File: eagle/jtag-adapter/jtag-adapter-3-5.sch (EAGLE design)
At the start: 40 parts, among them IC1 REG1117, Q1 BSS84, Q2 BSS123, X1 TAGCONNECT, X3 CC3220SF-JTAG-HAT, X5 JTAG-IN, X7 MICRO-USB-B

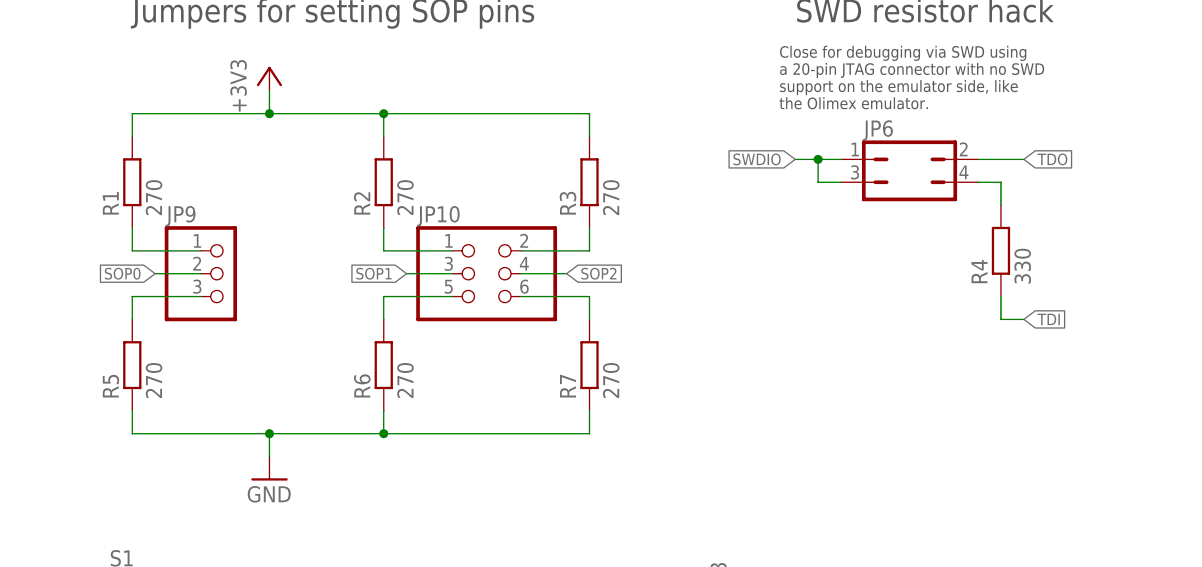
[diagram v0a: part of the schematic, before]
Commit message: Updates resistor values.
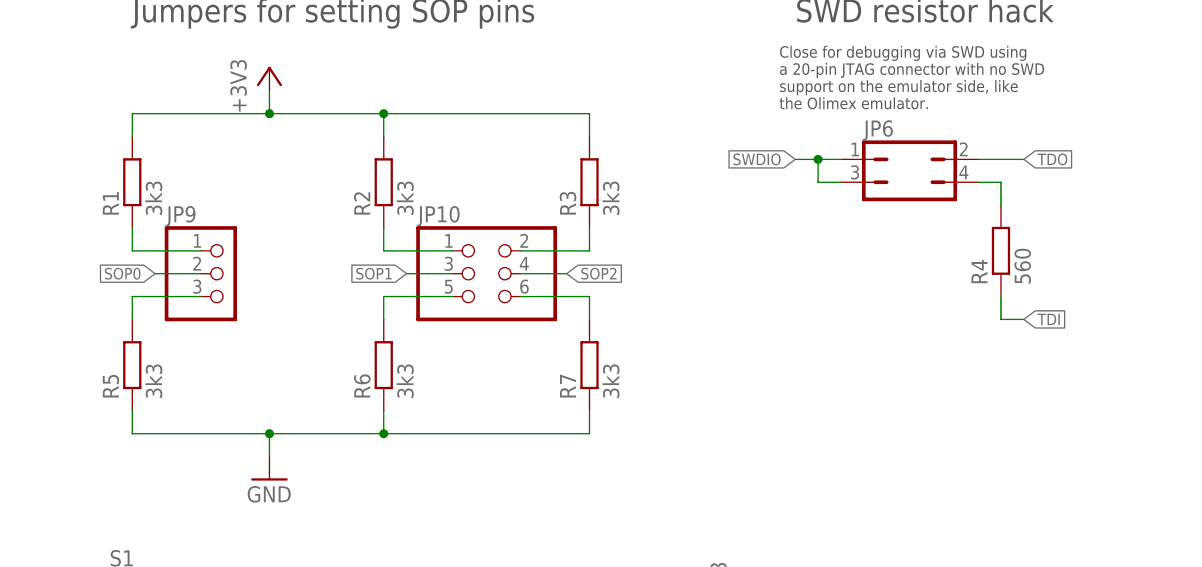
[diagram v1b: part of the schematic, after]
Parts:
- R1, R2, R3, R5, R6, R7: value 270 -> 3k3
- R4: value 330 -> 560
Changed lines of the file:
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@@
 <part name="FRAME1" library="tcs" deviceset="FRAME_A_L" device=""/>
 <part name="JP9" library="adafruit" deviceset="PINHD-1X3" device=""/>
-<part name="R1" library="rcl" library_urn="urn:adsk.eagle:library:334" deviceset="R-EU_" device="R0805" package3d_urn="urn:adsk.eagle:package:23553/2" value="270"/>
-<part name="R2" library="rcl" library_urn="urn:adsk.eagle:library:334" deviceset="R-EU_" device="R0805" package3d_urn="urn:adsk.eagle:package:23553/2" value="270"/>
-<part name="R3" library="rcl" library_urn="urn:adsk.eagle:library:334" deviceset="R-EU_" device="R0805" package3d_urn="urn:adsk.eagle:package:23553/2" value="270"/>
-<part name="R5" library="rcl" library_urn="urn:adsk.eagle:library:334" deviceset="R-EU_" device="R0805" package3d_urn="urn:adsk.eagle:package:23553/2" value="270"/>
-<part name="R6" library="rcl" library_urn="urn:adsk.eagle:library:334" deviceset="R-EU_" device="R0805" package3d_urn="urn:adsk.eagle:package:23553/2" value="270"/>
-<part name="R7" library="rcl" library_urn="urn:adsk.eagle:library:334" deviceset="R-EU_" device="R0805" package3d_urn="urn:adsk.eagle:package:23553/2" value="270"/>
+<part name="R1" library="rcl" library_urn="urn:adsk.eagle:library:334" deviceset="R-EU_" device="R0805" package3d_urn="urn:adsk.eagle:package:23553/2" value="3k3"/>
+<part name="R2" library="rcl" library_urn="urn:adsk.eagle:library:334" deviceset="R-EU_" device="R0805" package3d_urn="urn:adsk.eagle:package:23553/2" value="3k3"/>
+<part name="R3" library="rcl" library_urn="urn:adsk.eagle:library:334" deviceset="R-EU_" device="R0805" package3d_urn="urn:adsk.eagle:package:23553/2" value="3k3"/>
+<part name="R5" library="rcl" library_urn="urn:adsk.eagle:library:334" deviceset="R-EU_" device="R0805" package3d_urn="urn:adsk.eagle:package:23553/2" value="3k3"/>
+<part name="R6" library="rcl" library_urn="urn:adsk.eagle:library:334" deviceset="R-EU_" device="R0805" package3d_urn="urn:adsk.eagle:package:23553/2" value="3k3"/>
+<part name="R7" library="rcl" library_urn="urn:adsk.eagle:library:334" deviceset="R-EU_" device="R0805" package3d_urn="urn:adsk.eagle:package:23553/2" value="3k3"/>
 <part name="+3V32" library="supply1" library_urn="urn:adsk.eagle:library:371" deviceset="+3V3" device=""/>
 <part name="GND7" library="supply1" library_urn="urn:adsk.eagle:library:371" deviceset="GND" device=""/>
@@
 <part name="JP6" library="trainlib" deviceset="JP2Q" device=""/>
 <part name="JP7" library="trainlib" deviceset="JP3Q" device=""/>
-<part name="R4" library="rcl" library_urn="urn:adsk.eagle:library:334" deviceset="R-EU_" device="R0805" package3d_urn="urn:adsk.eagle:package:23553/2" value="330"/>
+<part name="R4" library="rcl" library_urn="urn:adsk.eagle:library:334" deviceset="R-EU_" device="R0805" package3d_urn="urn:adsk.eagle:package:23553/2" value="560"/>
 <part name="S3" library="trainlib" deviceset="TACTSW-6X6" device="" technology="S" value="FLASH"/>
 <part name="Q1" library="trainlib" deviceset="BSS84" device=""/>
